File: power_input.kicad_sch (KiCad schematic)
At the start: 100 parts, among them J201 61300211121, J202 61300211121, J203 61300211121, J204 61300211121, J205 61300211121, J206 61300211121, J207 61300211121, J208 61300211121, Q201 DMPH4029LFGQ, Q202 DMPH4029LFGQ, Q203 IRFL4315PbF, Q204 DMPH4029LFGQ, Q205 DMPH4029LFGQ, U201 LM4040-5.0, U202 TL331, U203 OPA197, U204 LM4040-5.0, U205 TL331, U206 LM4040-5.0, U207 TL331

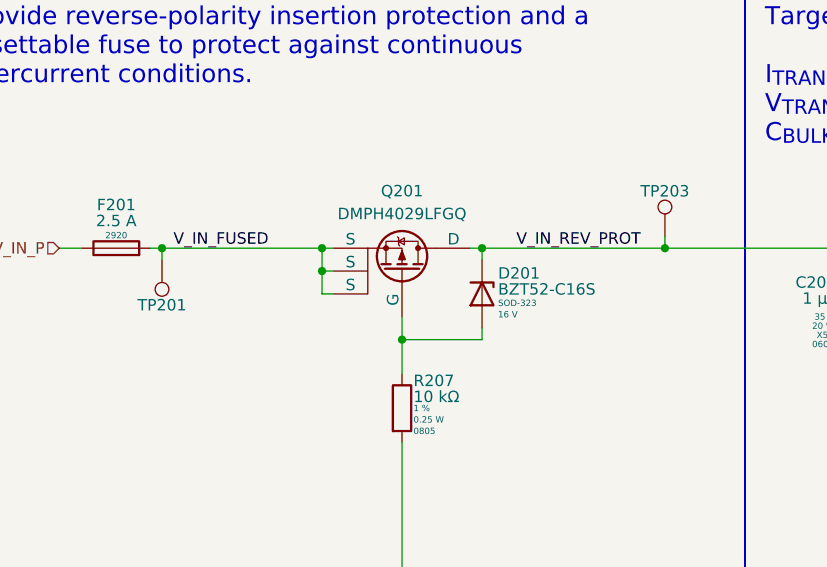
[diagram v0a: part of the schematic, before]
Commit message: Fix reverse polarity protection
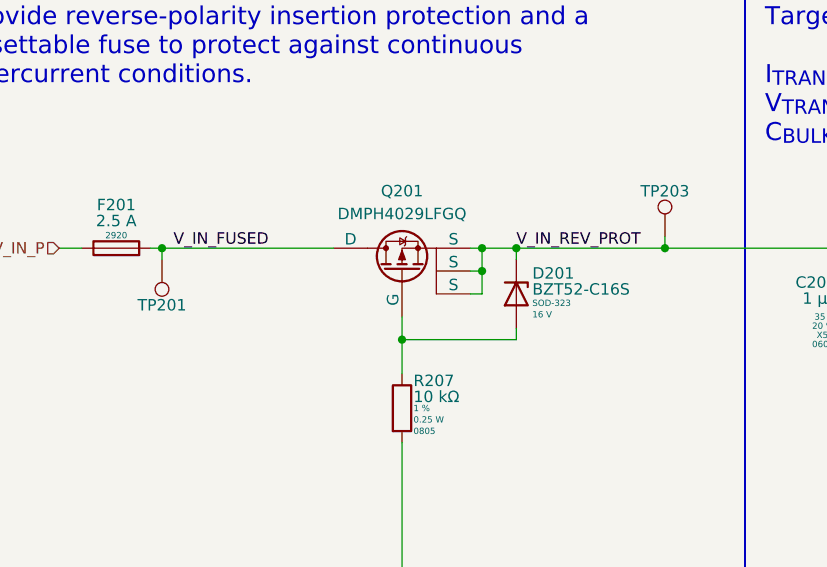
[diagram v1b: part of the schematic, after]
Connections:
- net V_IN_FUSED: now also Q201.5 (D); no longer Q201.1 (S), Q201.2 (S), Q201.3 (S)
- net V_IN_REV_PROT: now also Q201.1 (S), Q201.2 (S), Q201.3 (S); no longer Q201.5 (D)
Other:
- moved on the sheet: D201, Q201
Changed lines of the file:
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@@
 	)
 	(junction
-		(at 54.61 76.2)
-		(diameter 0)
-		(color 0 0 0 0)
-	)
-	(junction
 		(at 50.8 127)
 		(diameter 0)
@@
 	)
 	(junction
+		(at 72.39 78.74)
+		(diameter 0)
+		(color 0 0 0 0)
+	)
+	(junction
 		(at 73.66 177.8)
 		(diameter 0)
@@
 	)
 	(junction
+		(at 72.39 76.2)
+		(diameter 0)
+		(color 0 0 0 0)
+	)
+	(junction
 		(at 246.38 184.15)
 		(diameter 0)
@@
 	)
 	(junction
-		(at 54.61 78.74)
-		(diameter 0)
-		(color 0 0 0 0)
-	)
-	(junction
 		(at 304.8 114.3)
 		(diameter 0)
@@
 	)
 	(junction
+		(at 76.2 76.2)
+		(diameter 0)
+		(color 0 0 0 0)
+	)
+	(junction
 		(at 304.8 109.22)
 		(diameter 0)
@@
 	)
 	(junction
-		(at 72.39 76.2)
-		(diameter 0)
-		(color 0 0 0 0)
-	)
-	(junction
 		(at 153.67 76.2)
 		(diameter 0)
@@
 	(wire
 		(pts
-			(xy 72.39 85.09) (xy 72.39 86.36)
+			(xy 76.2 85.09) (xy 76.2 86.36)
 		)
 		(stroke
@@
 	(wire
 		(pts
-			(xy 54.61 78.74) (xy 55.88 78.74)
-		)
-		(stroke
-			(width 0)
-			(type default)
-		)
-	)
-	(wire
-		(pts
 			(xy 339.09 198.12) (xy 339.09 200.66)
 		)
@@
 	(wire
 		(pts
-			(xy 55.88 81.28) (xy 54.61 81.28)
-		)
-		(stroke
-			(width 0)
-			(type default)
-		)
-	)
-	(wire
-		(pts
 			(xy 21.59 177.8) (xy 21.59 186.69)
 		)
@@
 	(wire
 		(pts
-			(xy 54.61 78.74) (xy 54.61 76.2)
-		)
-		(stroke
-			(width 0)
-			(type default)
-		)
-	)
-	(wire
-		(pts
 			(xy 266.7 76.2) (xy 266.7 78.74)
 		)
@@
 	(wire
 		(pts
+			(xy 72.39 78.74) (xy 72.39 81.28)
+		)
+		(stroke
+			(width 0)
+			(type default)
+		)
+	)
+	(wire
+		(pts
 			(xy 383.54 76.2) (xy 387.35 76.2)
 		)
@@
 	(wire
 		(pts
+			(xy 71.12 81.28) (xy 72.39 81.28)
+		)
+		(stroke
+			(width 0)
+			(type default)
+		)
+	)
+	(wire
+		(pts
 			(xy 320.04 220.98) (xy 339.09 220.98)
 		)
@@
 	(wire
 		(pts
-			(xy 54.61 76.2) (xy 55.88 76.2)
+			(xy 36.83 76.2) (xy 55.88 76.2)
 		)
 		(stroke
@@
 	(wire
 		(pts
+			(xy 72.39 76.2) (xy 72.39 78.74)
+		)
+		(stroke
+			(width 0)
+			(type default)
+		)
+	)
+	(wire
+		(pts
 			(xy 342.9 76.2) (xy 342.9 77.47)
 		)
@@
 	(wire
 		(pts
+			(xy 71.12 78.74) (xy 72.39 78.74)
+		)
+		(stroke
+			(width 0)
+			(type default)
+		)
+	)
+	(wire
+		(pts
 			(xy 304.8 114.3) (xy 325.12 114.3)
 		)
@@
 	(wire
 		(pts
-			(xy 71.12 76.2) (xy 72.39 76.2)
-		)
-		(stroke
-			(width 0)
-			(type default)
-		)
-	)
-	(wire
-		(pts
 			(xy 59.69 186.69) (xy 59.69 184.15)
 		)
@@
 	(wire
 		(pts
-			(xy 54.61 81.28) (xy 54.61 78.74)
-		)
-		(stroke
-			(width 0)
-			(type default)
-		)
-	)
-	(wire
-		(pts
 			(xy 381 76.2) (xy 383.54 76.2)
 		)
@@
 	(wire
 		(pts
-			(xy 72.39 76.2) (xy 72.39 77.47)
+			(xy 229.87 213.36) (xy 241.3 213.36)
 		)
 		(stroke
@@
 	(wire
 		(pts
-			(xy 229.87 213.36) (xy 241.3 213.36)
+			(xy 152.4 208.28) (xy 168.91 208.28)
 		)
 		(stroke
@@
 	(wire
 		(pts
-			(xy 152.4 208.28) (xy 168.91 208.28)
+			(xy 76.2 76.2) (xy 76.2 77.47)
 		)
 		(stroke
@@
 	(wire
 		(pts
-			(xy 72.39 86.36) (xy 63.5 86.36)
+			(xy 76.2 86.36) (xy 63.5 86.36)
 		)
 		(stroke
@@
 	(wire
 		(pts
-			(xy 72.39 76.2) (xy 92.71 76.2)
+			(xy 71.12 76.2) (xy 72.39 76.2)
 		)
 		(stroke
@@
 	(wire
 		(pts
+			(xy 72.39 76.2) (xy 76.2 76.2)
+		)
+		(stroke
+			(width 0)
+			(type default)
+		)
+	)
+	(wire
+		(pts
 			(xy 304.8 177.8) (xy 311.15 177.8)
 		)
@@
 	(wire
 		(pts
+			(xy 76.2 76.2) (xy 92.71 76.2)
+		)
+		(stroke
+			(width 0)
+			(type default)
+		)
+	)
+	(wire
+		(pts
 			(xy 46.99 198.12) (xy 46.99 196.85)
 		)
@@
 	(wire
 		(pts
-			(xy 36.83 76.2) (xy 54.61 76.2)
-		)
-		(stroke
-			(width 0)
-			(type default)
-		)
-	)
-	(wire
-		(pts
 			(xy 139.7 86.36) (xy 139.7 127)
 		)
@@
 	(symbol
 		(lib_id "Device:D_Zener")
-		(at 72.39 81.28 270)
+		(at 76.2 81.28 270)
 		(unit 1)
 		(exclude_from_sim no)
@@
 		(dnp no)
 		(property "Reference" "D201"
-			(at 74.168 78.994 90)
+			(at 77.978 78.994 90)
 			(effects
 				(font
@@
 		)
 		(property "Value" "BZT52-C16S"
-			(at 74.168 80.772 90)
+			(at 77.978 80.772 90)
 			(effects
 				(font
@@
 		)
 		(property "Footprint" "Diode_SMD:D_SOD-323F"
-			(at 72.39 81.28 0)
+			(at 76.2 81.28 0)
 			(effects
 				(font
@@
 		)
 		(property "Datasheet" "https://www.panjit.com.tw/upload/datasheet/BZT52-C2V4S_SERIES.pdf"
-			(at 72.39 81.28 0)
+			(at 76.2 81.28 0)
 			(effects
 				(font
@@
 		)
 		(property "Description" "Zener Diode 16 V 200 mW ±5% Surface Mount SOD-323"
-			(at 72.39 81.28 0)
+			(at 76.2 81.28 0)
 			(effects
 				(font
@@
 		)
 		(property "Zener voltage" "16 V"
-			(at 74.168 83.566 90)
+			(at 77.978 83.566 90)
 			(effects
 				(font
@@
 		)
 		(property "MPN" "BZT52-C16S_R1_00001"
-			(at 72.39 81.28 90)
+			(at 76.2 81.28 90)
 			(effects
 				(font
@@
 		)
 		(property "Manufacturer" "Panjit International Inc."
-			(at 72.39 81.28 90)
+			(at 76.2 81.28 90)
 			(effects
 				(font
@@
 		)
 		(property "Digi-Key Part Number" "3757-BZT52-C16S_R1_00001CT-ND"
-			(at 72.39 81.28 90)
+			(at 76.2 81.28 90)
 			(effects
 				(font
@@
 		)
 		(property "Size" "SOD-323"
-			(at 74.168 82.296 90)
+			(at 77.978 82.296 90)
 			(effects
 				(font
@@
 	(symbol
 		(lib_id "Diodes Incorporated:Q_PMOS_DI3333-8")
-		(at 63.5 78.74 270)
-		(mirror x)
+		(at 63.5 78.74 90)
 		(unit 1)
 		(exclude_from_sim no)
@@
 		)
 		(property "Footprint" "Package_SON:Diodes_PowerDI3333-8"
-			(at 61.722 73.66 0)
+			(at 65.278 73.66 0)
 			(effects
 				(font
@@
 		)
 		(property "Datasheet" "https://www.diodes.com/assets/Datasheets/DMPH4029LFGQ.pdf"
-			(at 61.722 73.66 0)
+			(at 65.278 73.66 0)
 			(effects
 				(font
@@
 		)
 		(property "Description" "P-Channel 40 V 8A (Ta), 22A (Tc) 1.2W (Ta) Surface Mount POWERDI3333-8"
-			(at 61.722 73.66 0)
+			(at 65.278 73.66 0)
 			(effects
 				(font
@@
 		)
 		(property "Manufacturer" "Diodes Incorporated"
-			(at 61.722 73.66 0)
+			(at 65.278 73.66 0)
 			(effects
 				(font
@@
 		)
 		(property "MPN" "DMPH4029LFGQ-7"
-			(at 61.722 73.66 0)
+			(at 65.278 73.66 0)
 			(effects
 				(font

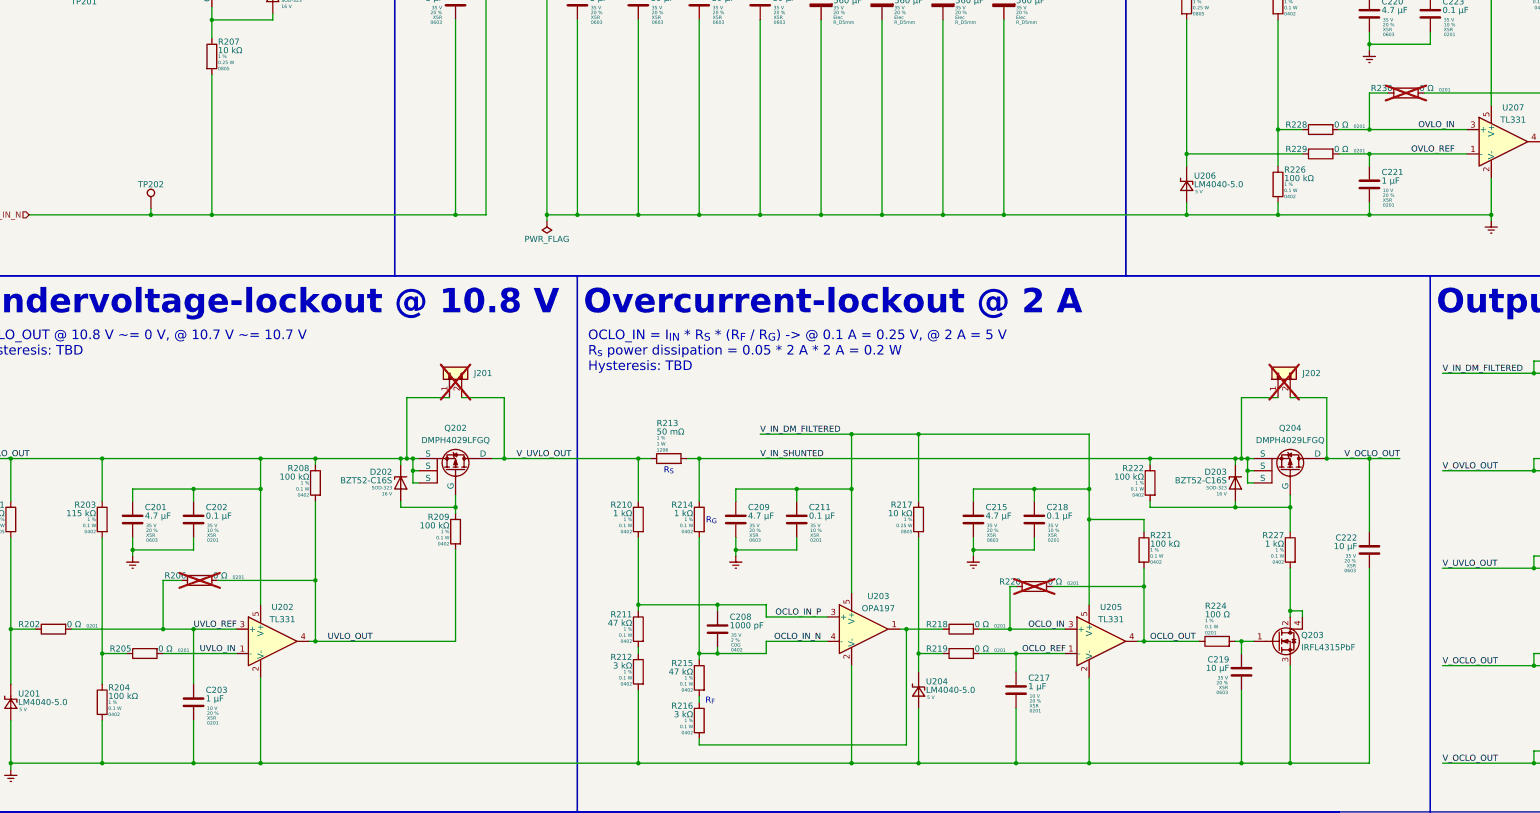
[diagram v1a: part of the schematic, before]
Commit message: Adjust power section passive sizes
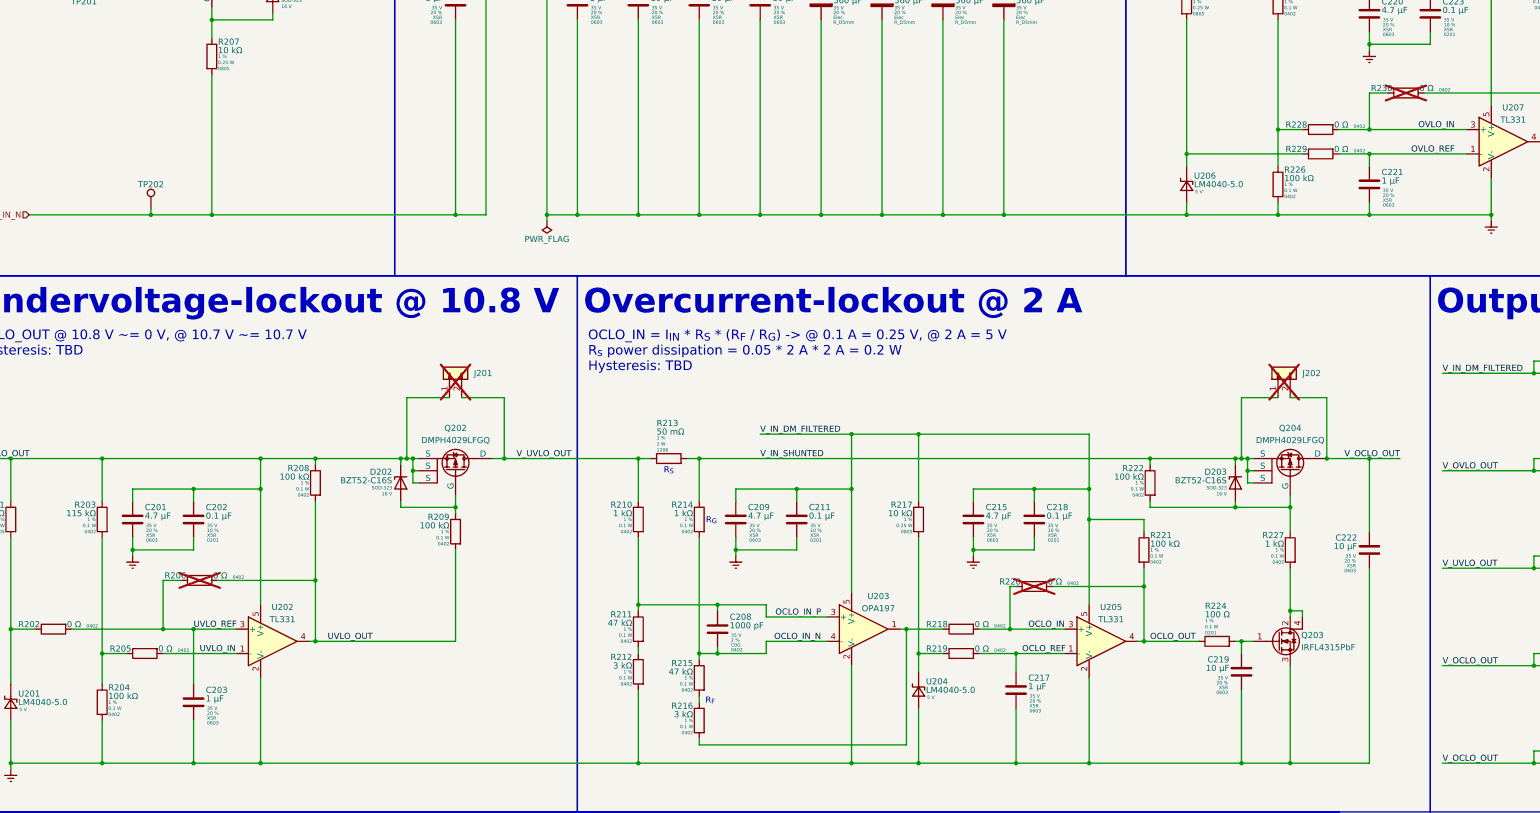
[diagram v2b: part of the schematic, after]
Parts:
- C203, C217, C221: footprint perfect_footprints:C_0201_0603Metric -> Capacitor_SMD:C_0603_1608Metric; Digi-Key Part Number 1276-1324-1-ND -> 490-12330-1-ND; MPN CL03A105MP3NSNC -> GRT188R61H105KE13D; Manufacturer Samsung Electro-Mechanics -> Murata Electronics; Size 0201 -> 0603; Voltage rating 10 V -> 35 V
- R202, R205, R206, R218, R219, R220, R228, R229, R230: footprint perfect_footprints:R_0201_0603Metric -> perfect_footprints:R_0402_1005Metric_HDI; Digi-Key Part Number P15979CT-ND -> P0.0JCT-ND; MPN ERJ-1GN0R00C -> ERJ-2GE0R00X; Size 0201 -> 0402

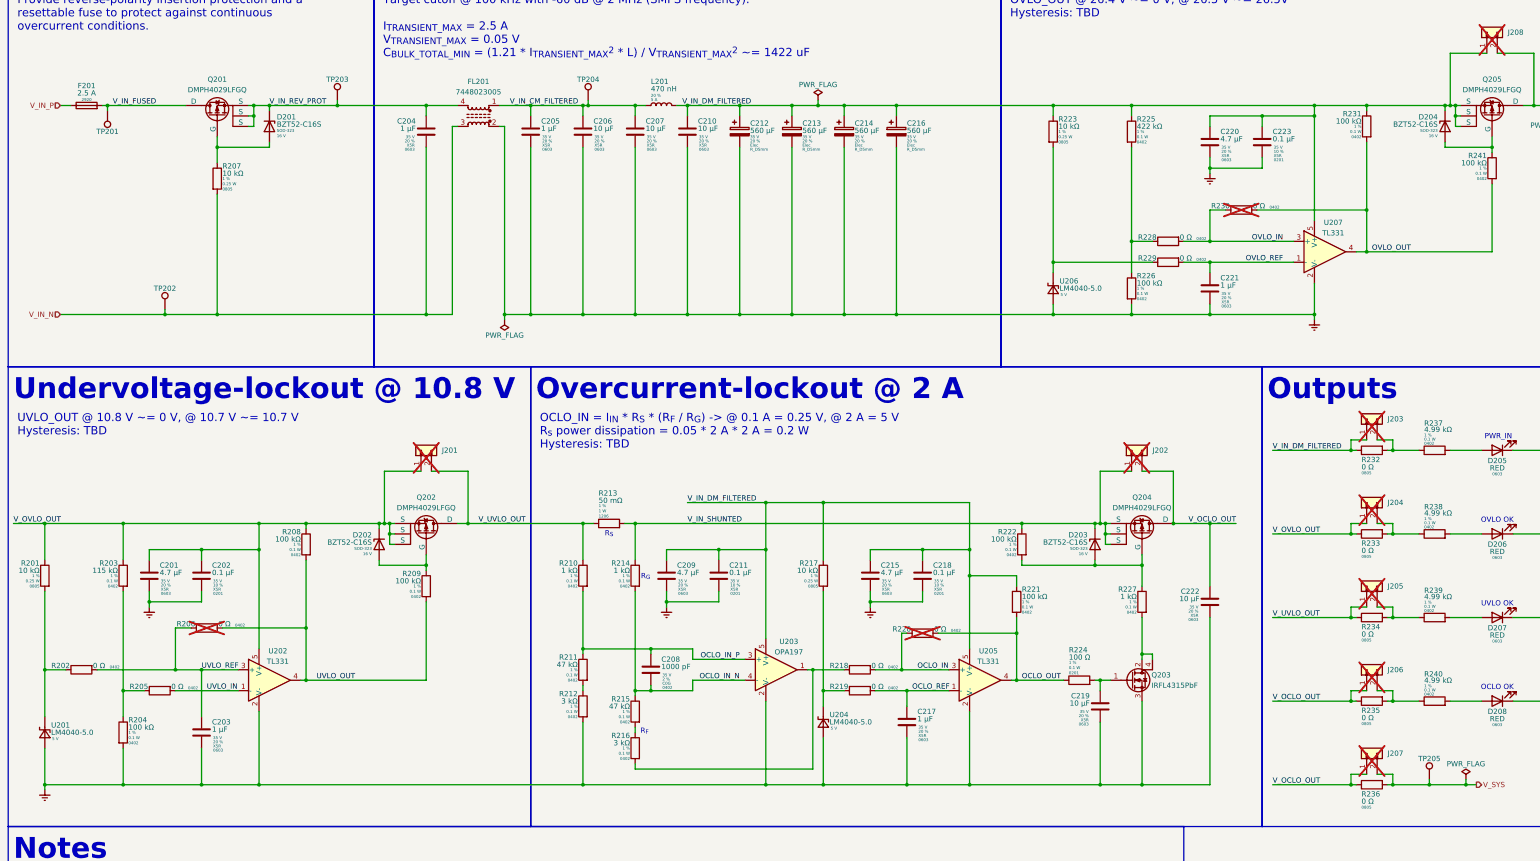
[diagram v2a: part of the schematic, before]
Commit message: Remove redundant test points
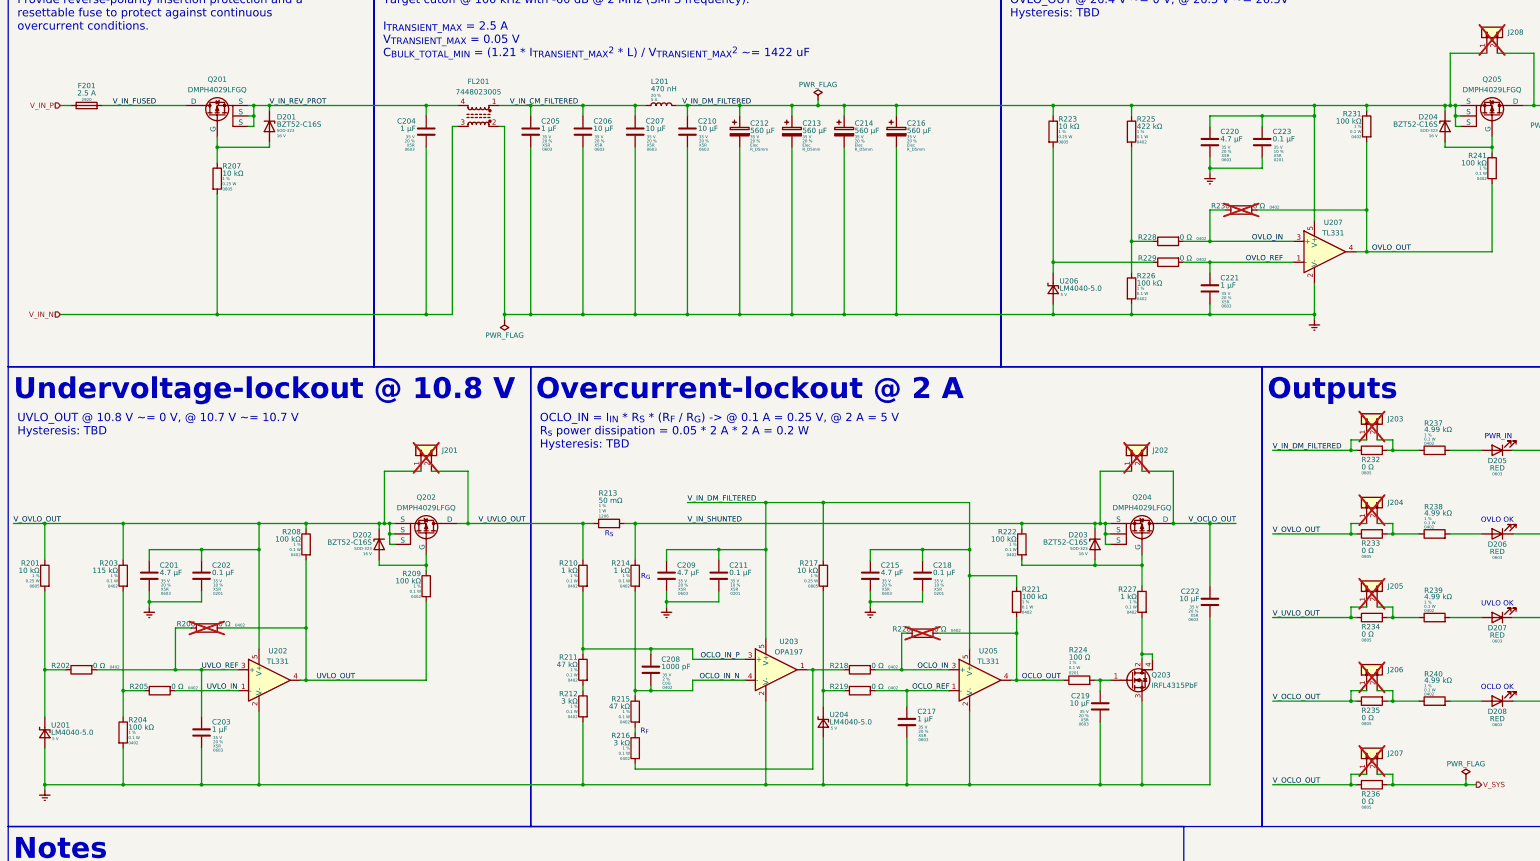
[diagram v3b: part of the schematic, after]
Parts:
- removed TP201, TP202, TP203, TP204, TP205: TestPoint, TestPoint:TestPoint_Pad_D1.0mm, symbol Connector:TestPoint

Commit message: Fix OCLO
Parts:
- C208: value 1000 pF -> 3300 pF; footprint perfect_footprints:C_0402_1005Metric_HDI -> perfect_footprints:C_0201_0603Metric; Digi-Key Part Number 490-3244-1-ND -> 490-GRM033R71E332KA12JCT-ND; MPN GRM1555C1H102JA01D -> GRM033R71E332KA12J; Size 0402 -> 0201; Temperature coefficient C0G -> X7R; Tolerance 2 % -> 10 %; Voltage rating 35 V -> 25 V
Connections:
- net OCLO_IN: now also C217.1, R219.2, U205.1 (-); no longer R218.2, R220.1, U205.3 (+)
- net OCLO_REF: now also R218.2, R220.1, U205.3 (+); no longer C217.1, R219.2, U205.1 (-)
- net at R217.2, U204.1 (K): now also R218.1; no longer R219.1
- net at R216.2, U203.1: now also R219.1; no longer R218.1
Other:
- moved on the sheet: C217
